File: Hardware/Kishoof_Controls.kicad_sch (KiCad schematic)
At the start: 25 parts, among them J10 USB_C_Receptacle, J11 Conn_01x02_Pin, J12 Conn_01x01_Socket, J3 WavetablePosA, J4 WavetablePosB, J5 WarpCV, J6 VOct, J7 VCA, J8 Audio_Out_L, J9 Audio_Out_R, SW1 SW_Push, SW2 Mode_Switch, SW3 Octave_Switch, SW4 ChB_Output, SW5 Encoder

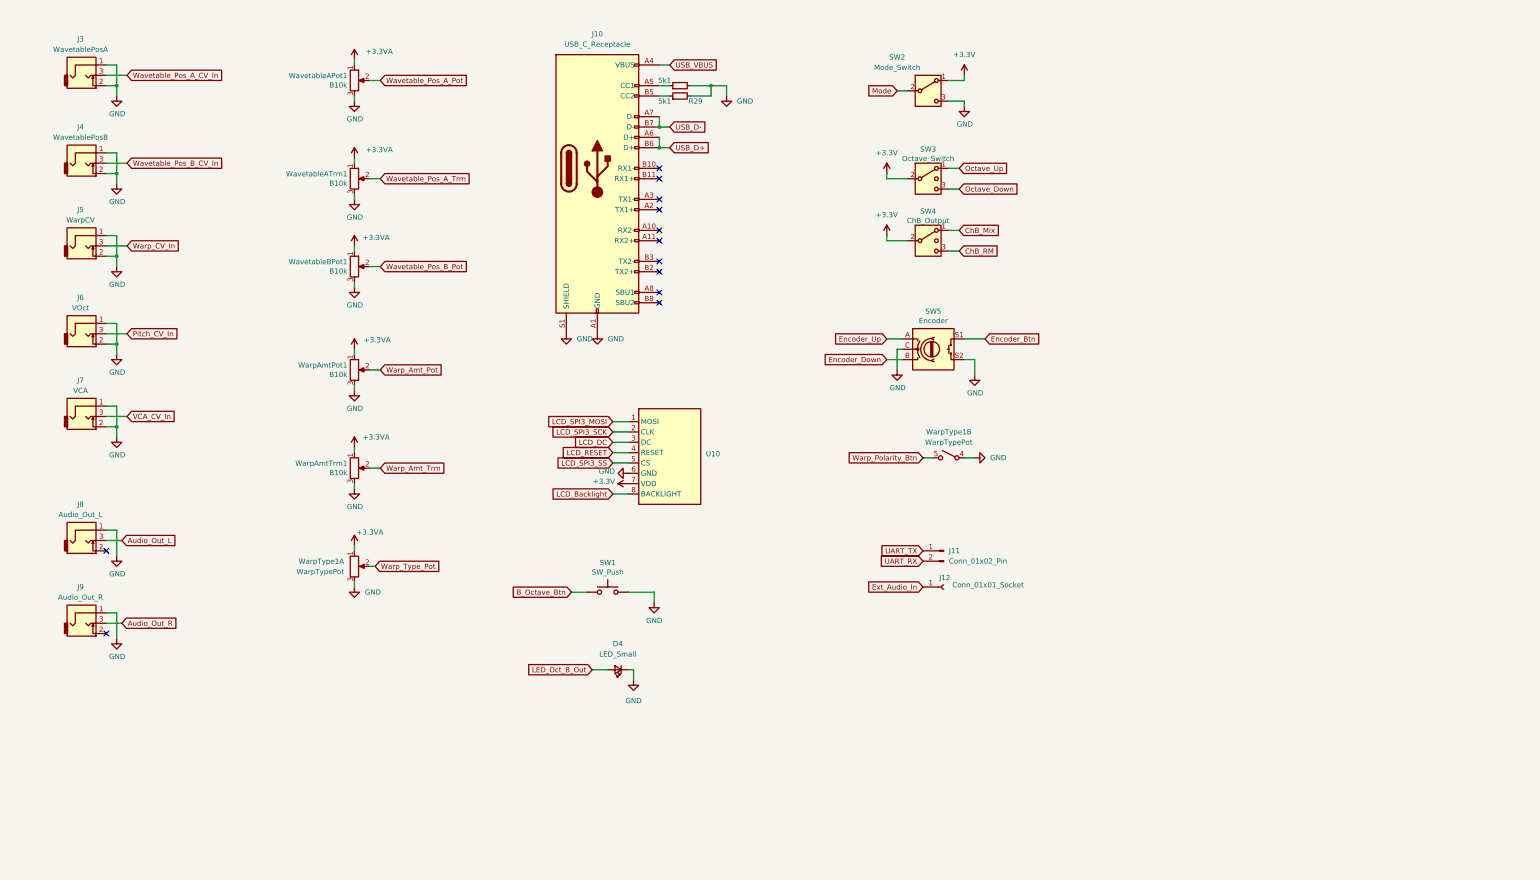
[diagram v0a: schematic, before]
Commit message: Separated PCB controls and components
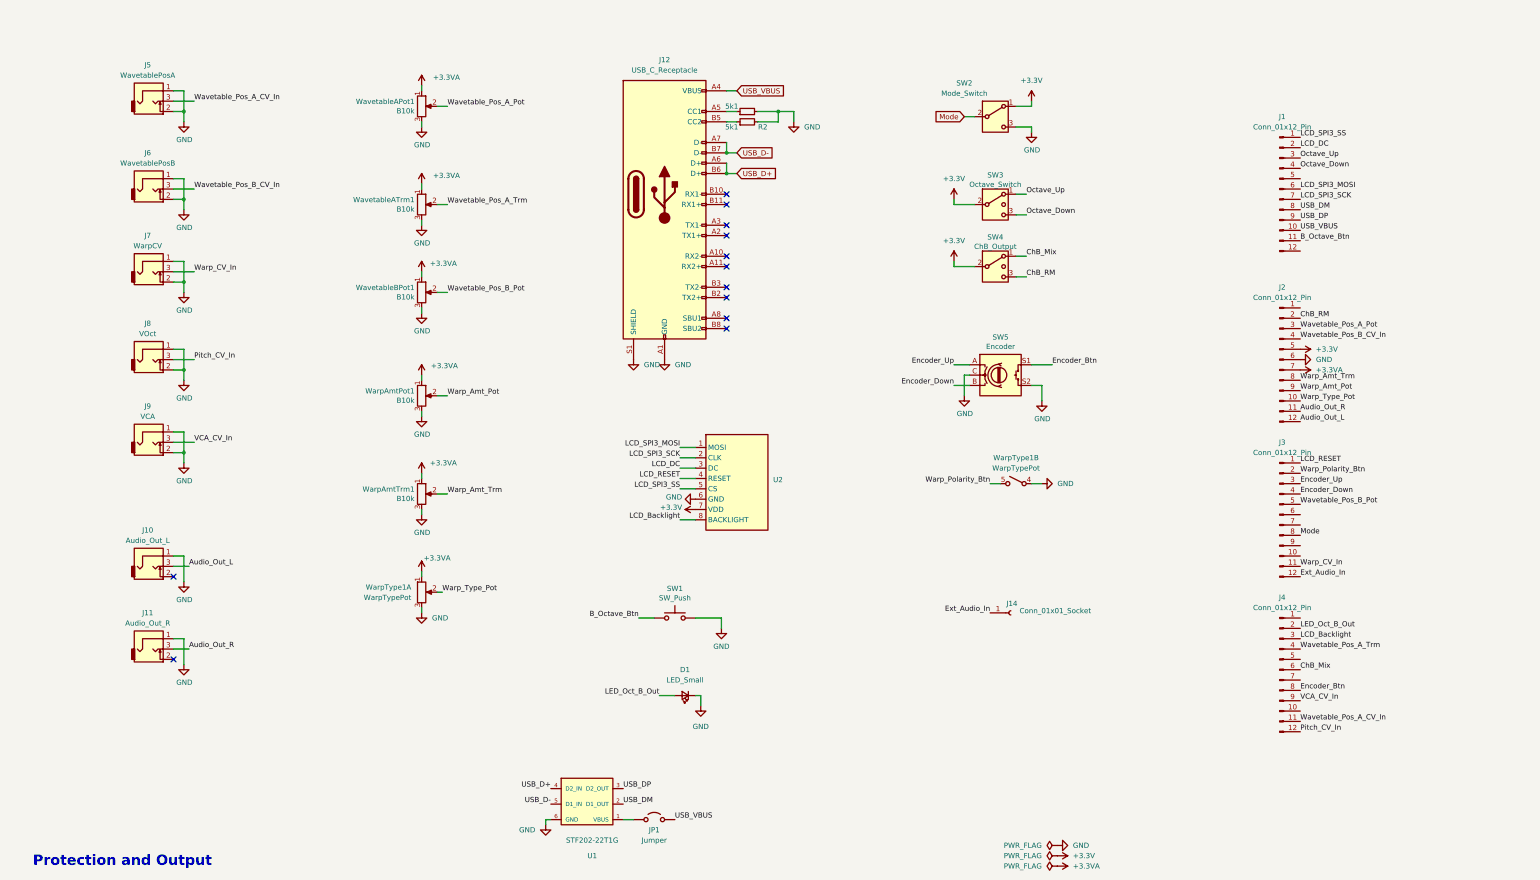
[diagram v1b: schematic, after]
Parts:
- removed D4: LED_Small, LED_THT:LED_D3.0mm_FlatTop, symbol Device:LED_Small
- removed J10: USB_C_Receptacle, Custom_Footprints:USB_C_Receptacle_Amphenol_12401951E412A, symbol Connector:USB_C_Receptacle
- removed J11: Conn_01x02_Pin, Connector_PinHeader_2.54mm:PinHeader_1x02_P2.54mm_Vertical, symbol Connector:Conn_01x02_Pin
- removed J12: Conn_01x01_Socket, Connector_PinHeader_2.54mm:PinHeader_1x01_P2.54mm_Vertical, symbol Connector:Conn_01x01_Socket
- removed J3: WavetablePosA, Custom_Footprints:THONKICONN_hole, symbol thonkiconn:AudioJack2_Ground_Switch
- removed J4: WavetablePosB, Custom_Footprints:THONKICONN_hole, symbol thonkiconn:AudioJack2_Ground_Switch
- removed R28, R29: 5k1, Resistor_SMD:R_0603_1608Metric, symbol Device:R_Small
- removed U10: ~, Custom_Footprints:LCD_Riser, symbol Mountjoy:LCD_Riser
- added D1: LED_Small, LED_THT:LED_D3.0mm_FlatTop, symbol Device:LED_Small
- added J1, J2, J3, J4: Conn_01x12_Pin, Connector_PinSocket_2.54mm:PinSocket_1x12_P2.54mm_Vertical, symbol Connector:Conn_01x12_Pin
- added J10: Audio_Out_L, Custom_Footprints:THONKICONN_hole, symbol thonkiconn:AudioJack2_Ground_Switch
- added J11: Audio_Out_R, Custom_Footprints:THONKICONN_hole, symbol thonkiconn:AudioJack2_Ground_Switch
- added J12: USB_C_Receptacle, Custom_Footprints:USB_C_Receptacle_Amphenol_12401951E412A, symbol Connector:USB_C_Receptacle
- added J14: Conn_01x01_Socket, Connector_PinHeader_2.54mm:PinHeader_1x01_P2.54mm_Vertical, symbol Connector:Conn_01x01_Socket
- added JP1: Jumper, Jumper:SolderJumper-2_P1.3mm_Open_RoundedPad1.0x1.5mm, symbol Jumper:Jumper_2_Open
- added R1, R2: 5k1, Resistor_SMD:R_0603_1608Metric, symbol Device:R_Small
- added U1: STF202-22T1G, Custom_Footprints:STF202-22T1G, symbol STF202-22T1G:STF202-22T1G
- added U2: ~, Custom_Footprints:LCD_Riser, symbol Mountjoy:LCD_Riser
- J5: value WarpCV -> WavetablePosA
- J6: value VOct -> WavetablePosB
- J7: value VCA -> WarpCV
- J8: value Audio_Out_L -> VOct
- J9: value Audio_Out_R -> VCA
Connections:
- net +3.3V: now also J2.5 (Pin_5), U2.7 (VDD)
- net +3.3VA: now also J2.7 (Pin_7)
- net Audio_Out_L: now also J10.3, J2.12 (Pin_12); no longer J8.3
- net Audio_Out_R: now also J11.3, J2.11 (Pin_11); no longer J9.3
- net B_Octave_Btn: now also J1.11 (Pin_11)
- net ChB_Mix: now also J4.6 (Pin_6)
- net ChB_RM: now also J2.2 (Pin_2)
- net Encoder_Btn: now also J4.8 (Pin_8)
- net Encoder_Down: now also J3.4 (Pin_4)
- net Encoder_Up: now also J3.3 (Pin_3)
- net Ext_Audio_In: now also J14.1 (Pin_1), J3.12 (Pin_12)
- net GND: now also J8.2, J9.2, D1.1 (K), J10.1, J11.1, J12.A1 (GND), J12.A12 (GND), J12.B1 (GND), J12.B12 (GND), J12.S1 (SHIELD), J2.6 (Pin_6), R1.2, R2.2, U1.6 (GND), U2.6 (GND)
- net LCD_Backlight: now also J4.3 (Pin_3), U2.8 (BACKLIGHT)
- net LCD_DC: now also J1.2 (Pin_2), U2.3 (DC)
- net LCD_RESET: now also J3.1 (Pin_1), U2.4 (RESET)
- net LCD_SPI3_MOSI: now also J1.6 (Pin_6), U2.1 (MOSI)
- net LCD_SPI3_SCK: now also J1.7 (Pin_7), U2.2 (CLK)
- net LCD_SPI3_SS: now also J1.1 (Pin_1), U2.5 (CS)
- net LED_Oct_B_Out: now also D1.2 (A), J4.2 (Pin_2)
- net Mode: now also J3.8 (Pin_8)
- net Octave_Down: now also J1.4 (Pin_4)
- net Octave_Up: now also J1.3 (Pin_3)
- net Pitch_CV_In: now also J8.3, J4.12 (Pin_12); no longer J6.3
- net USB_D+: now also J12.A6 (D+), J12.B6 (D+), U1.4 (D2_IN)
- net USB_D-: now also J12.A7 (D-), J12.B7 (D-), U1.5 (D1_IN)
- net USB_VBUS: now also J1.10 (Pin_10), J12.A4 (VBUS), J12.A9 (VBUS), J12.B4 (VBUS), J12.B9 (VBUS), JP1.2 (B)
- net VCA_CV_In: now also J9.3, J4.9 (Pin_9); no longer J7.3
- net Warp_Amt_Pot: now also J2.9 (Pin_9)
- net Warp_Amt_Trm: now also J2.8 (Pin_8)
- net Warp_CV_In: now also J7.3, J3.11 (Pin_11); no longer J5.3
- net Warp_Polarity_Btn: now also J3.2 (Pin_2)
- net Warp_Type_Pot: now also J2.10 (Pin_10)
- net Wavetable_Pos_A_CV_In: now also J5.3, J4.11 (Pin_11)
- net Wavetable_Pos_A_Pot: now also J2.3 (Pin_3)
- net Wavetable_Pos_A_Trm: now also J4.4 (Pin_4)
- net Wavetable_Pos_B_CV_In: now also J6.3, J2.4 (Pin_4)
- net Wavetable_Pos_B_Pot: now also J3.5 (Pin_5)
- new net: JP1.1 (A), U1.1 (VBUS)
- new net: J12.A5 (CC1), R1.1
- new net: J12.B5 (CC2), R2.1
- new net USB_DM: J1.8 (Pin_8), U1.2 (D1_OUT)
- new net USB_DP: J1.9 (Pin_9), U1.3 (D2_OUT)
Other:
- note added: "Protection and Output"
- company: (none) -> Mountjoy Modular
- title: (none) -> Kishoof Components

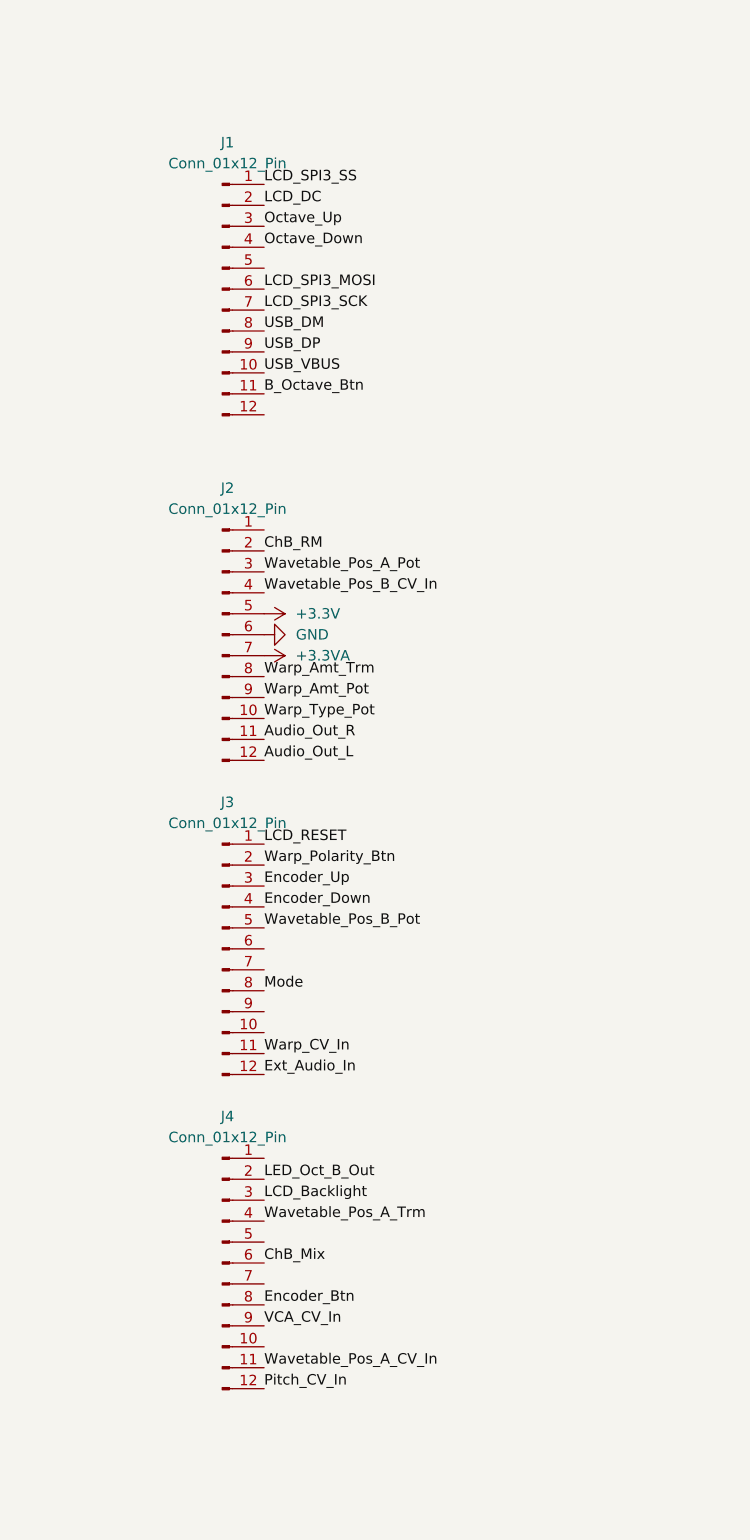
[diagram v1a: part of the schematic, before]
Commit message: Control board routed; updated lcd riser
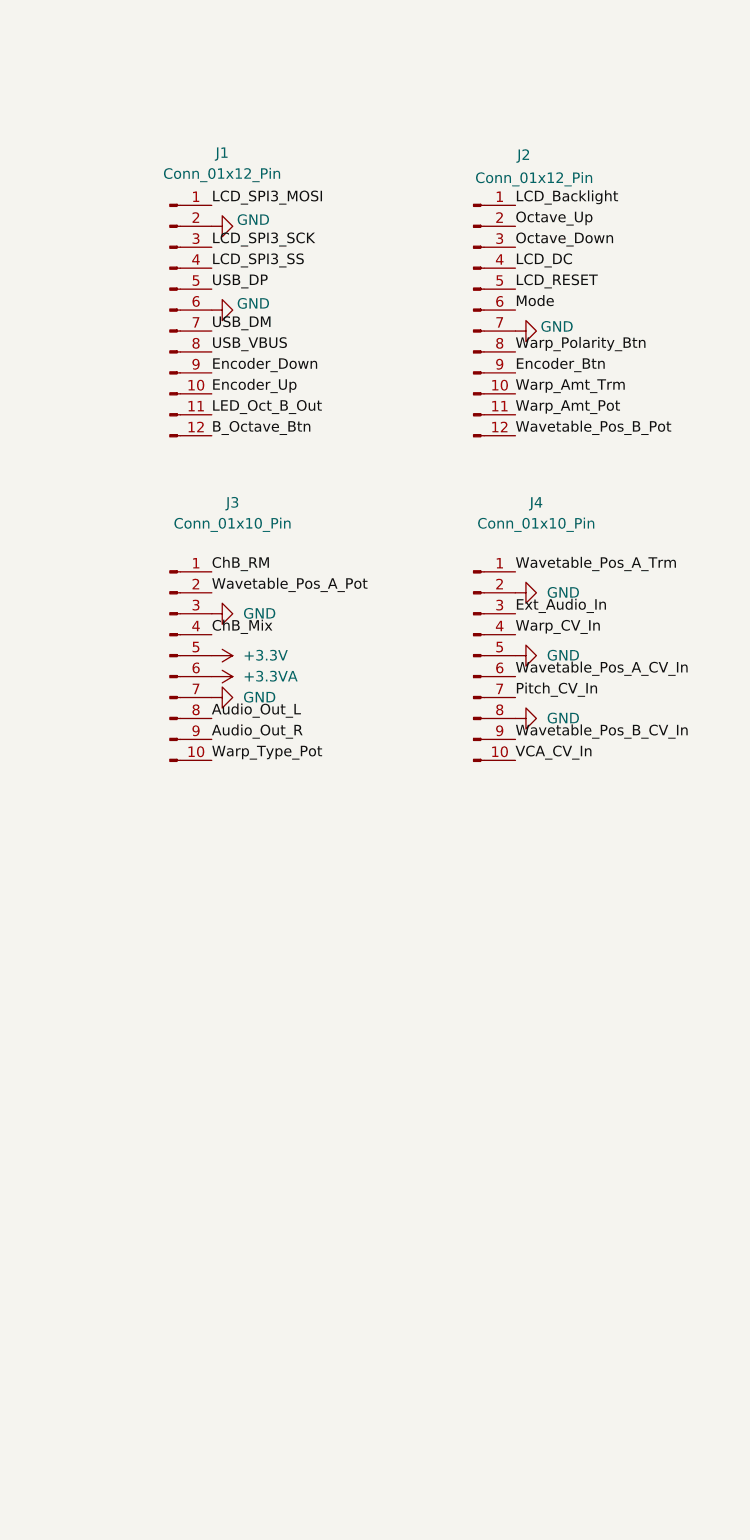
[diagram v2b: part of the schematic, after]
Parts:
- removed J3, J4: Conn_01x12_Pin, Connector_PinSocket_2.54mm:PinSocket_1x12_P2.54mm_Vertical, symbol Connector:Conn_01x12_Pin
- added J3, J4: Conn_01x10_Pin, Connector_PinSocket_2.54mm:PinSocket_1x10_P2.54mm_Vertical, symbol Connector:Conn_01x10_Pin
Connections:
- net +3.3V: now also J3.5 (Pin_5); no longer J2.5 (Pin_5)
- net +3.3VA: now also J3.6 (Pin_6); no longer J2.7 (Pin_7)
- net Audio_Out_L: now also J3.8 (Pin_8); no longer J2.12 (Pin_12)
- net Audio_Out_R: now also J3.9 (Pin_9); no longer J2.11 (Pin_11)
- net B_Octave_Btn: now also J1.12 (Pin_12); no longer J1.11 (Pin_11)
- net ChB_Mix: now also J3.4 (Pin_4)
- net ChB_RM: now also J3.1 (Pin_1); no longer J2.2 (Pin_2)
- net Encoder_Btn: now also J2.9 (Pin_9)
- net Encoder_Down: now also J1.9 (Pin_9)
- net Encoder_Up: now also J1.10 (Pin_10)
- net Ext_Audio_In: now also J4.3 (Pin_3)
- net GND: now also J1.2 (Pin_2), J1.6 (Pin_6), J2.7 (Pin_7), J3.3 (Pin_3), J3.7 (Pin_7), J4.2 (Pin_2), J4.5 (Pin_5), J4.8 (Pin_8); no longer J2.6 (Pin_6)
- net LCD_Backlight: now also J2.1 (Pin_1)
- net LCD_DC: now also J2.4 (Pin_4); no longer J1.2 (Pin_2)
- net LCD_RESET: now also J2.5 (Pin_5)
- net LCD_SPI3_MOSI: now also J1.1 (Pin_1); no longer J1.6 (Pin_6)
- net LCD_SPI3_SCK: now also J1.3 (Pin_3); no longer J1.7 (Pin_7)
- net LCD_SPI3_SS: now also J1.4 (Pin_4); no longer J1.1 (Pin_1)
- net LED_Oct_B_Out: now also J1.11 (Pin_11)
- net Mode: now also J2.6 (Pin_6)
- net Octave_Down: now also J2.3 (Pin_3); no longer J1.4 (Pin_4)
- net Octave_Up: now also J2.2 (Pin_2); no longer J1.3 (Pin_3)
- net Pitch_CV_In: now also J4.7 (Pin_7)
- net USB_DM: now also J1.7 (Pin_7); no longer J1.8 (Pin_8)
- net USB_DP: now also J1.5 (Pin_5); no longer J1.9 (Pin_9)
- net USB_VBUS: now also J1.8 (Pin_8); no longer J1.10 (Pin_10)
- net VCA_CV_In: now also J4.10 (Pin_10)
- net Warp_Amt_Pot: now also J2.11 (Pin_11); no longer J2.9 (Pin_9)
- net Warp_Amt_Trm: now also J2.10 (Pin_10); no longer J2.8 (Pin_8)
- net Warp_CV_In: now also J4.4 (Pin_4)
- net Warp_Polarity_Btn: now also J2.8 (Pin_8)
- net Warp_Type_Pot: now also J3.10 (Pin_10); no longer J2.10 (Pin_10)
- net Wavetable_Pos_A_CV_In: now also J4.6 (Pin_6)
- net Wavetable_Pos_A_Pot: now also J3.2 (Pin_2); no longer J2.3 (Pin_3)
- net Wavetable_Pos_A_Trm: now also J4.1 (Pin_1)
- net Wavetable_Pos_B_CV_In: now also J4.9 (Pin_9); no longer J2.4 (Pin_4)
- net Wavetable_Pos_B_Pot: now also J2.12 (Pin_12)
